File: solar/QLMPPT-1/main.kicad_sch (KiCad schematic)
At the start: 0 parts

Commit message: Continuing QLMPPT-1
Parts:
- added D1, D6: MIC 20A10, symbol Device:D
- added FH?: 15A, symbol Device:Fuse_Small
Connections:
- new net BAT+: D6.1 (K), FH?.1
- new net BAT-: D6.2 (A)
- new net PV+: D1.1 (K)
- new net PV-: D1.2 (A)
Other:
- sheet Untitled Sheet renamed Boost converter
- sheet Boost converter: file untitled.kicad_sch -> boost.kicad_sch
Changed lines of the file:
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@@
 (kicad_sch (version 20211123) (generator eeschema)
   (paper "A4")
-  (sheet (at 91.44 48.895) (size 24.13 24.13) (fields_autoplaced)
+  (junction (at 58.42 63.5) (diameter 0) (color 0 0 0 0)
+  )
+  (wire (pts (xy 48.895 54.61) (xy 58.42 54.61))
+    (stroke (width 0) (type default) (color 0 0 0 0))
+  )
+  (wire (pts (xy 50.165 63.5) (xy 58.42 63.5))
+    (stroke (width 0) (type default) (color 0 0 0 0))
+  )
+  (wire (pts (xy 58.42 63.5) (xy 58.42 64.135))
+    (stroke (width 0) (type default) (color 0 0 0 0))
+  )
+  (wire (pts (xy 48.895 46.99) (xy 58.42 46.99))
+    (stroke (width 0) (type default) (color 0 0 0 0))
+  )
+  (wire (pts (xy 58.42 63.5) (xy 68.58 63.5))
+    (stroke (width 0) (type default) (color 0 0 0 0))
+  )
+  (wire (pts (xy 50.165 71.755) (xy 58.42 71.755))
+    (stroke (width 0) (type default) (color 0 0 0 0))
+  )
+  (global_label "BAT+" (shape bidirectional) (at 50.165 63.5 180) (fields_autoplaced)
+    (effects (font (size 1.27 1.27)) (justify right))
+    (property "Intersheet References" "${INTERSHEET_REFS}" (id 0) (at 42.8533 63.5794 0)
+      (effects (font (size 1.27 1.27)) (justify right) hide)
+    )
+  )
+  (global_label "BAT-" (shape bidirectional) (at 50.165 71.755 180) (fields_autoplaced)
+    (effects (font (size 1.27 1.27)) (justify right))
+    (property "Intersheet References" "${INTERSHEET_REFS}" (id 0) (at 42.8533 71.8344 0)
+      (effects (font (size 1.27 1.27)) (justify right) hide)
+    )
+  )
+  (global_label "PV-" (shape bidirectional) (at 48.895 54.61 180) (fields_autoplaced)
+    (effects (font (size 1.27 1.27)) (justify right))
+    (property "Intersheet References" "${INTERSHEET_REFS}" (id 0) (at 42.5509 54.6894 0)
+      (effects (font (size 1.27 1.27)) (justify right) hide)
+    )
+  )
+  (global_label "PV+" (shape bidirectional) (at 48.895 46.99 180) (fields_autoplaced)
+    (effects (font (size 1.27 1.27)) (justify right))
+    (property "Intersheet References" "${INTERSHEET_REFS}" (id 0) (at 42.5509 47.0694 0)
+      (effects (font (size 1.27 1.27)) (justify right) hide)
+    )
+  )
+  (symbol (lib_id "Device:D") (at 58.42 50.8 270) (unit 1)
+    (in_bom yes) (on_board yes) (fields_autoplaced)
+    (property "Reference" "D1" (id 0) (at 60.452 49.9653 90)
+      (effects (font (size 1.27 1.27)) (justify left))
+    )
+    (property "Value" "MIC 20A10" (id 1) (at 60.452 52.5022 90)
+      (effects (font (size 1.27 1.27)) (justify left))
+    )
+    (property "Footprint" "" (id 2) (at 58.42 50.8 0)
+      (effects (font (size 1.27 1.27)) hide)
+    )
+    (property "Datasheet" "~" (id 3) (at 58.42 50.8 0)
+      (effects (font (size 1.27 1.27)) hide)
+    )
+    (pin "1")
+    (pin "2")
+  )
+  (symbol (lib_id "Device:D") (at 58.42 67.945 270) (unit 1)
+    (in_bom yes) (on_board yes) (fields_autoplaced)
+    (property "Reference" "D6" (id 0) (at 60.452 67.1103 90)
+      (effects (font (size 1.27 1.27)) (justify left))
+    )
+    (property "Value" "MIC 20A10" (id 1) (at 60.452 69.6472 90)
+      (effects (font (size 1.27 1.27)) (justify left))
+    )
+    (property "Footprint" "" (id 2) (at 58.42 67.945 0)
+      (effects (font (size 1.27 1.27)) hide)
+    )
+    (property "Datasheet" "~" (id 3) (at 58.42 67.945 0)
+      (effects (font (size 1.27 1.27)) hide)
+    )
+    (pin "1")
+    (pin "2")
+  )
+  (symbol (lib_id "Device:Fuse_Small") (at 71.12 63.5 0) (unit 1)
+    (in_bom yes) (on_board yes) (fields_autoplaced)
+    (property "Reference" "FH?" (id 0) (at 71.12 59.4192 0))
+    (property "Value" "15A" (id 1) (at 71.12 61.9561 0))
+    (property "Footprint" "" (id 2) (at 71.12 63.5 0)
+      (effects (font (size 1.27 1.27)) hide)
+    )
+    (property "Datasheet" "~" (id 3) (at 71.12 63.5 0)
+      (effects (font (size 1.27 1.27)) hide)
+    )
+    (pin "1")
+    (pin "2")
+  )
+  (sheet (at 120.65 46.99) (size 24.13 24.13) (fields_autoplaced)
     (stroke (width 0.1524) (type solid) (color 0 0 0 0))
     (fill (color 0 0 0 0.0000))
-    (property "Sheet name" "Untitled Sheet" (id 0) (at 91.44 48.1834 0)
+    (property "Sheet name" "Boost converter" (id 0) (at 120.65 46.2784 0)
       (effects (font (size 1.27 1.27)) (justify left bottom))
     )
-    (property "Sheet file" "untitled.kicad_sch" (id 1) (at 91.44 73.6096 0)
+    (property "Sheet file" "boost.kicad_sch" (id 1) (at 120.65 71.7046 0)
       (effects (font (size 1.27 1.27)) (justify left top))
     )
@@
     (path "/2eff0aea-dd55-4aef-ab94-2b855006b99e" (page "2"))
   )
+  (symbol_instances
+    (path "/2eff0aea-dd55-4aef-ab94-2b855006b99e/01c9db67-46b5-4a2a-b314-0fe067678f39"
+      (reference "C5") (unit 1) (value "100V,220uF") (footprint "")
+    )
+    (path "/2eff0aea-dd55-4aef-ab94-2b855006b99e/be9f5b88-6f56-452e-9b38-e3ea426375a9"
+      (reference "C8") (unit 1) (value "100V,220uF") (footprint "")
+    )
+    (path "/2eff0aea-dd55-4aef-ab94-2b855006b99e/4f02867a-7c2f-4c41-b9bd-b4958cb5319c"
+      (reference "C21") (unit 1) (value "100V,220uF") (footprint "")
+    )
+    (path "/2eff0aea-dd55-4aef-ab94-2b855006b99e/9da221f1-1007-4516-aa9e-7091cca33f29"
+      (reference "C24") (unit 1) (value "100V,220uF") (footprint "")
+    )
+    (path "/a47a7d51-523c-4842-807c-f4d682e78e5c"
+      (reference "D1") (unit 1) (value "MIC 20A10") (footprint "")
+    )
+    (path "/a76babda-7962-431d-b6d7-5ed48a547e14"
+      (reference "D6") (unit 1) (value "MIC 20A10") (footprint "")
+    )
+    (path "/e91eaaea-362f-4451-976d-b5ecc78683c7"
+      (reference "FH?") (unit 1) (value "15A") (footprint "")
+    )
+    (path "/2eff0aea-dd55-4aef-ab94-2b855006b99e/a6520adb-7357-4ce3-b912-ecfc735d2ccf"
+      (reference "L1") (unit 1) (value "Power choke") (footprint "")
+    )
+  )
 )

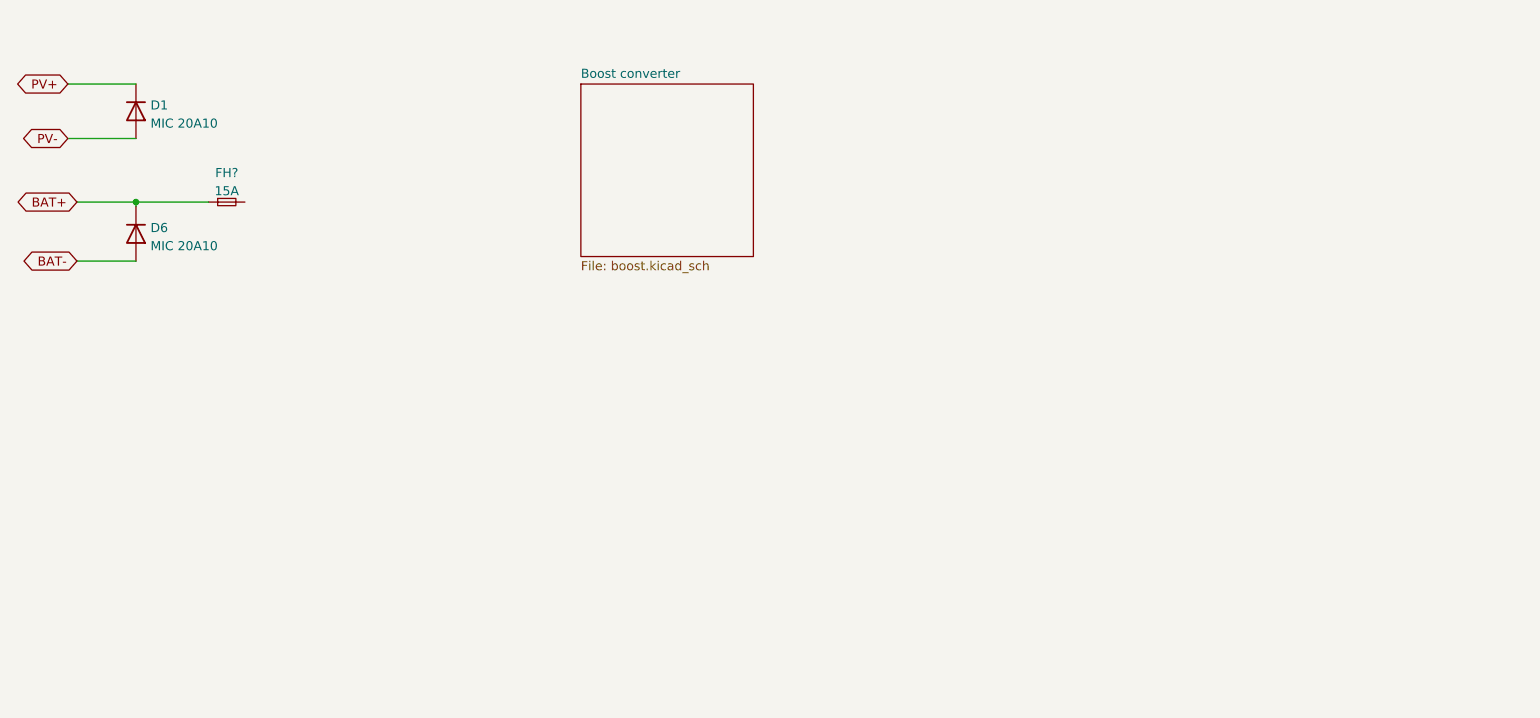
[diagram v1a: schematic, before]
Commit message: Sketching boost converter
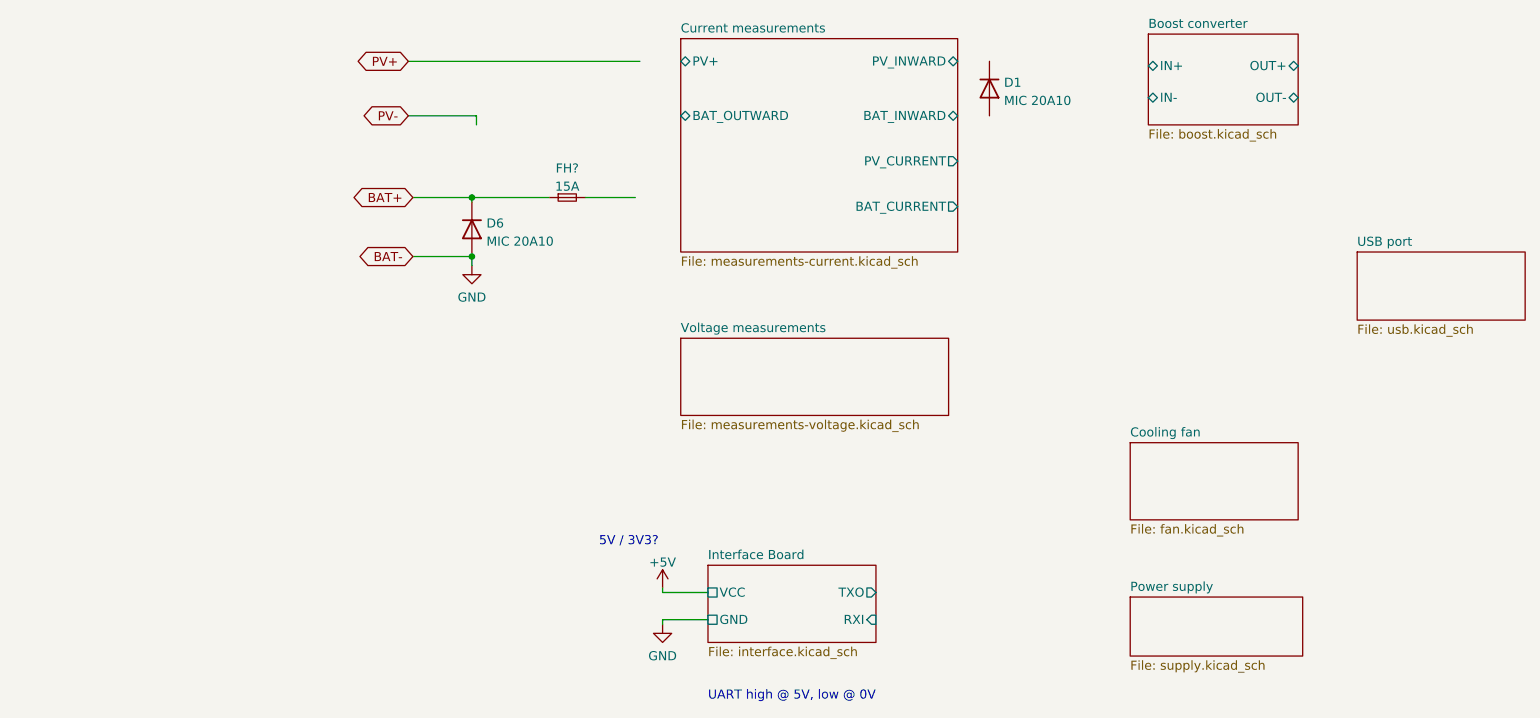
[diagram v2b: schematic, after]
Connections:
- net PV+: no longer D1.1 (K)
- net PV-: no longer D1.2 (A)
- net BAT- renamed GND
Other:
- added sheet Cooling fan (fan.kicad_sch)
- added sheet Current measurements (measurements-current.kicad_sch)
- added sheet Interface Board (interface.kicad_sch)
- added sheet Power supply (supply.kicad_sch)
- added sheet USB port (usb.kicad_sch)
- added sheet Voltage measurements (measurements-voltage.kicad_sch)
- sheet Boost converter ports: added IN+, IN-, OUT+, OUT-; removed none
- note added: "5V / 3V3?"
- note added: "UART high @ 5V, low @ 0V"
- moved on the sheet: D1, D6, FH?

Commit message: Continuing QLMPPT-1
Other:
- sheet Interface Board renamed Interface Daughter Board
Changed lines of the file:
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@@
     (pin "2")
   )
-  (sheet (at 229.235 70.485) (size 23.495 9.525) (fields_autoplaced)
+  (sheet (at 201.295 70.485) (size 23.495 9.525) (fields_autoplaced)
     (stroke (width 0.1524) (type solid) (color 0 0 0 0))
     (fill (color 0 0 0 0.0000))
-    (property "Sheet name" "USB port" (id 0) (at 229.235 69.7734 0)
+    (property "Sheet name" "USB port" (id 0) (at 201.295 69.7734 0)
       (effects (font (size 1.27 1.27)) (justify left bottom))
     )
-    (property "Sheet file" "usb.kicad_sch" (id 1) (at 229.235 80.5946 0)
+    (property "Sheet file" "usb.kicad_sch" (id 1) (at 201.295 80.5946 0)
       (effects (font (size 1.27 1.27)) (justify left top))
     )
   )
-  (sheet (at 138.43 114.3) (size 23.495 10.795) (fields_autoplaced)
+  (sheet (at 138.43 114.3) (size 27.305 11.43) (fields_autoplaced)
     (stroke (width 0.1524) (type solid) (color 0 0 0 0))
     (fill (color 0 0 0 0.0000))
-    (property "Sheet name" "Interface Board" (id 0) (at 138.43 113.5884 0)
+    (property "Sheet name" "Interface Daughter Board" (id 0) (at 138.43 113.5884 0)
       (effects (font (size 1.27 1.27)) (justify left bottom))
     )
-    (property "Sheet file" "interface.kicad_sch" (id 1) (at 138.43 125.6796 0)
+    (property "Sheet file" "interface.kicad_sch" (id 1) (at 138.43 126.3146 0)
       (effects (font (size 1.27 1.27)) (justify left top))
     )
@@
       (effects (font (size 1.27 1.27)) (justify left))
     )
-    (pin "TXO" output (at 161.925 118.11 0)
+    (pin "TXO" output (at 165.735 118.11 0)
       (effects (font (size 1.27 1.27)) (justify right))
     )
-    (pin "RXI" input (at 161.925 121.92 0)
+    (pin "RXI" input (at 165.735 121.92 0)
       (effects (font (size 1.27 1.27)) (justify right))
     )
